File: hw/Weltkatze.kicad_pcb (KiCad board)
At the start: 2 copper layers, 120 x 120 mm, 13 parts, among them U1 ESP32-C6-MINI-1/U

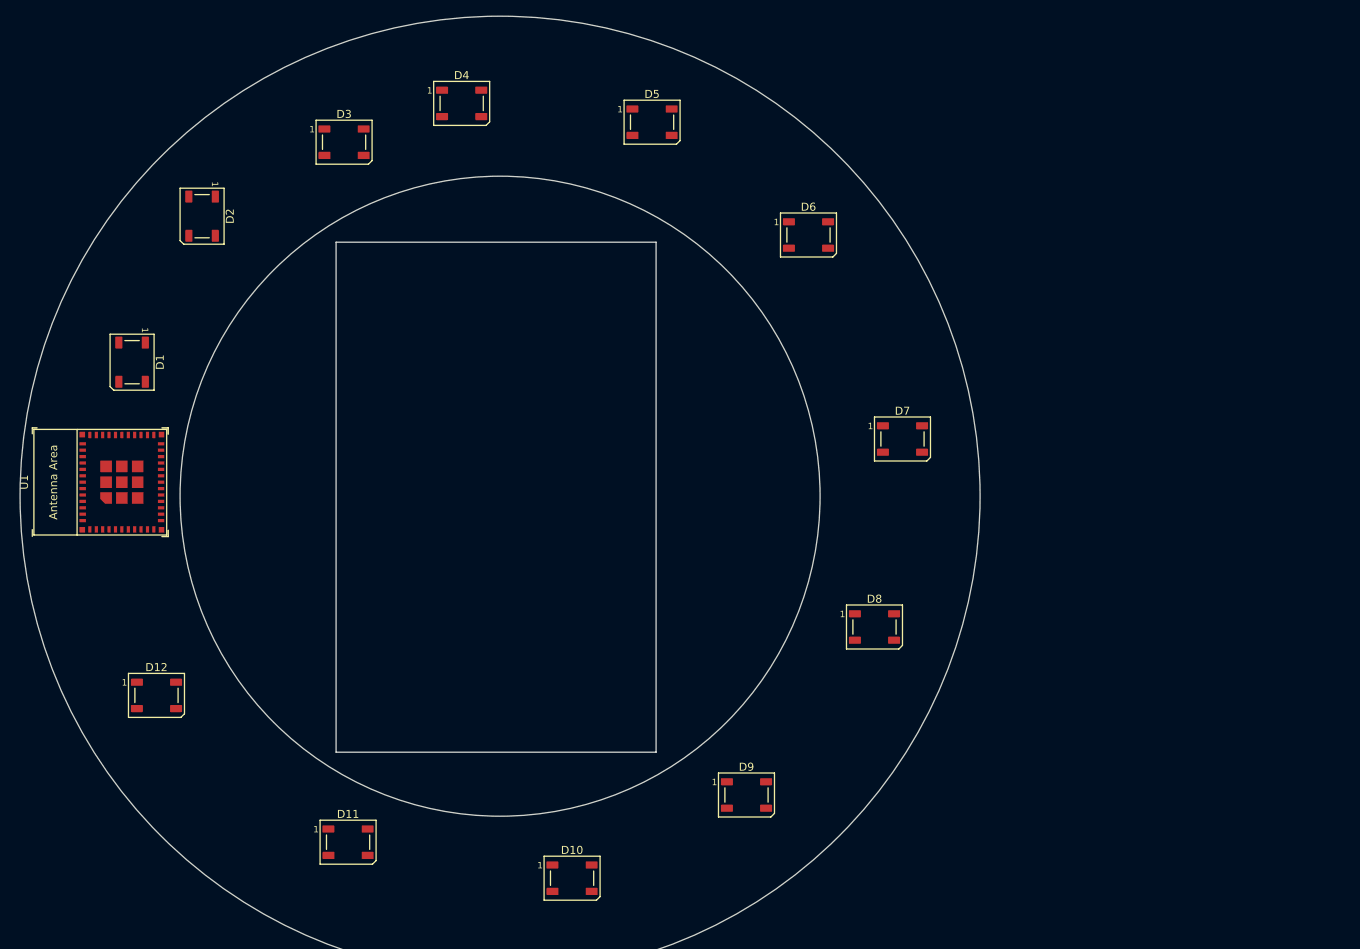
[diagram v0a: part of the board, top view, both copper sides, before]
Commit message: Work on footprinting and PCB
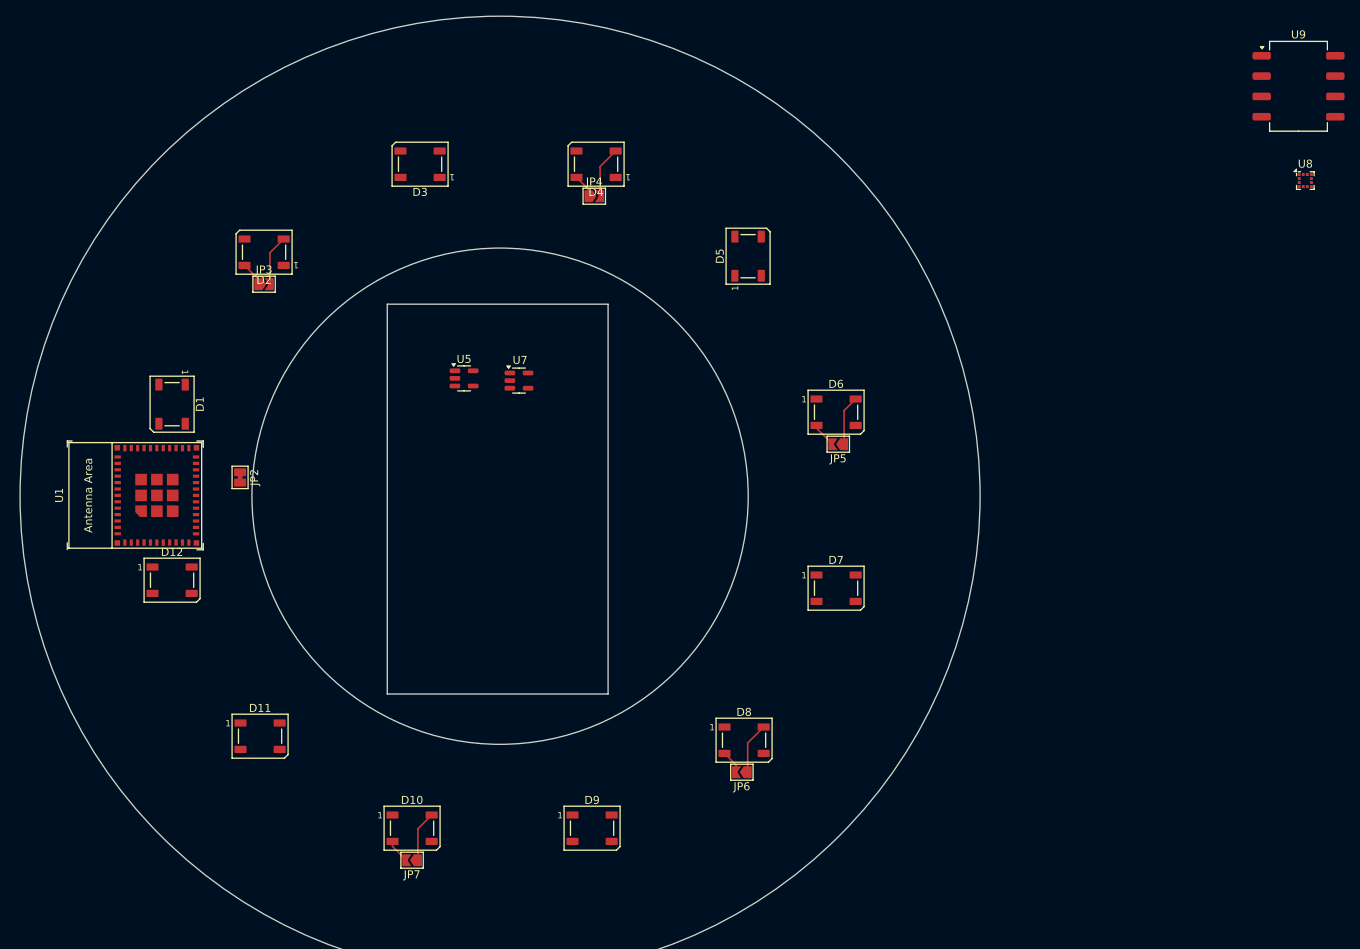
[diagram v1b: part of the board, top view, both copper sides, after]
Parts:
- added JP2: DBG_UART, Jumper:SolderJumper-2_P1.3mm_Bridged_Pad1.0x1.5mm, F.Cu at (98.5, 99.2)
- added JP3: SolderJumper_2_Open, Jumper:SolderJumper-2_P1.3mm_Open_TrianglePad1.0x1.5mm, F.Cu at (101.5, 75.0)
- added JP4: SolderJumper_2_Open, Jumper:SolderJumper-2_P1.3mm_Open_TrianglePad1.0x1.5mm, F.Cu at (142.8, 64.0)
- added JP5: SolderJumper_2_Open, Jumper:SolderJumper-2_P1.3mm_Open_TrianglePad1.0x1.5mm, F.Cu at (173.3, 95.0)
- added JP6: SolderJumper_2_Open, Jumper:SolderJumper-2_P1.3mm_Open_TrianglePad1.0x1.5mm, F.Cu at (161.2, 136.0)
- added JP7: SolderJumper_2_Open, Jumper:SolderJumper-2_P1.3mm_Open_TrianglePad1.0x1.5mm, F.Cu at (120.0, 147.0)
- added U5: SPX3819M5-L-3-3, Package_TO_SOT_SMD:SOT-23-5, F.Cu at (126.5, 86.8)
- added U7: SPX3819M5-L-3-3, Package_TO_SOT_SMD:SOT-23-5, F.Cu at (133.4, 87.0)
- added U8: SC7A20, Package_LGA:LGA-12_2x2mm_P0.5mm, F.Cu at (231.7, 62.0)
- added U9: XGZP6897D, Sensor_Pressure:CFSensor_XGZP6897x, F.Cu at (230.8, 50.3)
- moved D6 22.4 mm to (173.0, 91.0)
- moved D8 21.6 mm to (161.5, 132.0)
- moved D10 21.0 mm to (120.0, 143.0)
- moved D5 20.6 mm to (162.0, 71.5), turned to 90 degrees
- moved D7 20.4 mm to (173.0, 113.0)
- moved D9 19.7 mm to (142.5, 143.0)
- moved D4 18.4 mm to (143.0, 60.0), turned to 180 degrees
- moved D11 17.2 mm to (101.0, 131.5)
- moved D12 14.5 mm to (90.0, 112.0)
- moved D3 9.89 mm to (121.0, 60.0), turned to 180 degrees
- moved D2 8.96 mm to (101.5, 71.0), turned to 180 degrees
- moved D1 7.25 mm to (90.0, 90.0)
- moved U1 4.68 mm to (85.4, 101.4)
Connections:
- net /LEDs/5V renamed +5V
- net Net-(U1-EN/CHIP_PU) renamed /Logic/ESP_RST
- D12 pad 2: unconnected-(D12-DOUT-Pad2) -> Net-(D12-DOUT)
- U1 pad 10: unconnected-(U1-MTDI/GPIO5/ADC1_CH5-Pad10) -> Net-(J3-Pin_3)
- U1 pad 12: unconnected-(U1-GPIO0/ADC1_CH0/XTAL_32K_P-Pad12) -> /Logic/XTAL_P
- U1 pad 13: unconnected-(U1-GPIO1/ADC1_CH1/XTAL_32K_N-Pad13) -> /Logic/XTAL_N
- U1 pad 15: unconnected-(U1-MTCK/GPIO6/ADC1_CH6-Pad15) -> Net-(J3-Pin_2)
- U1 pad 16: unconnected-(U1-MTDO/GPIO7-Pad16) -> Net-(J3-Pin_1)
- U1 pad 17: unconnected-(U1-GPIO12/USB_D--Pad17) -> /Logic/USB_DM
- U1 pad 18: unconnected-(U1-GPIO13/USB_D+-Pad18) -> /Logic/USB_DP
- U1 pad 19: unconnected-(U1-GPIO14-Pad19) -> /Logic/ESP_SCL
- U1 pad 20: unconnected-(U1-GPIO15-Pad20) -> /Logic/ESP_SDA
- U1 pad 22: unconnected-(U1-GPIO8-Pad22) -> Net-(U1-GPIO8)
- U1 pad 23: unconnected-(U1-GPIO9-Pad23) -> /Logic/ESP_BOOT
- U1 pad 28: unconnected-(U1-GPIO22-Pad28) -> /LEDs/LED_DIN
- U1 pad 30: unconnected-(U1-U0RXD/GPIO17-Pad30) -> /Logic/UART_RX
- U1 pad 31: unconnected-(U1-U0TXD/GPIO16-Pad31) -> /Logic/UART_TX
- U1 pad 6: unconnected-(U1-GPIO3/ADC1_CH3-Pad6) -> /Logic/VBAT_MON
- U1 pad 9: unconnected-(U1-MTMS/GPIO4/ADC1_CH4-Pad9) -> Net-(J3-Pin_4)
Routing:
- net Net-(D7-DOUT): track 0.00 -> 6.48 mm
- net Net-(D4-DOUT): track 0.00 -> 6.46 mm
- net Net-(D10-DIN): track 0.00 -> 6.36 mm
- net Net-(D2-DOUT): track 0.00 -> 6.36 mm
- net Net-(D5-DOUT): track 0.00 -> 6.25 mm
- net Net-(D6-DOUT): track 0.00 -> 3.18 mm
- net Net-(D10-DOUT): track 0.00 -> 3.06 mm
- net Net-(D1-DOUT): track 0.00 -> 3.06 mm
- net Net-(D3-DOUT): track 0.00 -> 2.97 mm
- net Net-(D8-DOUT): track 0.00 -> 2.95 mm
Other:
- outline, holes or cut-outs redrawn

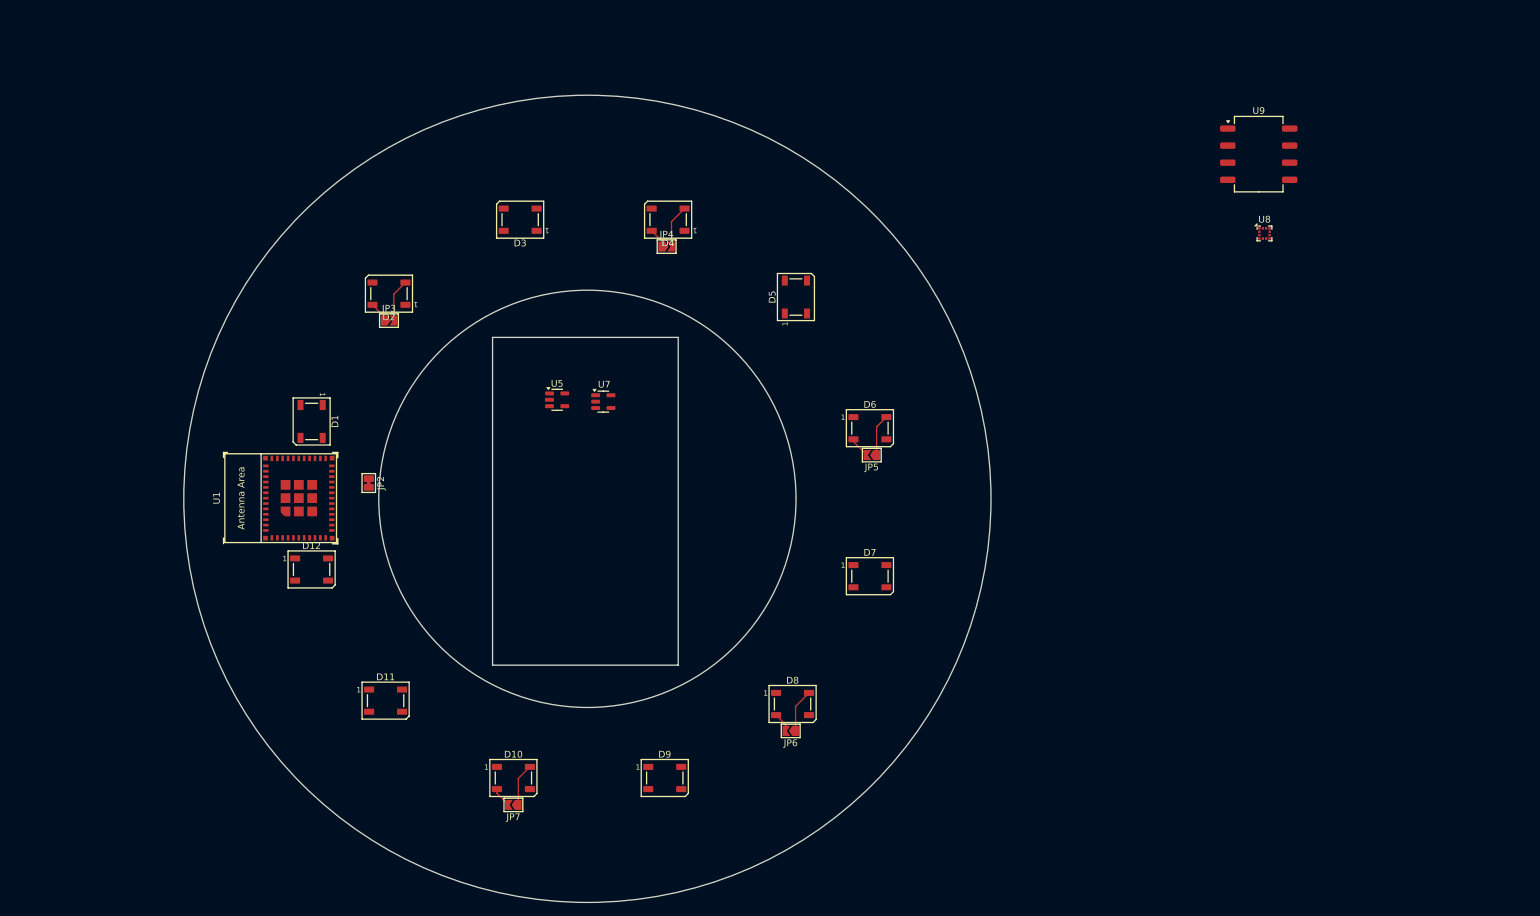
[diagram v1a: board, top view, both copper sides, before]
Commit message: Footprinting, begin layout
I've assigned all the footprints except a few, so I've started on layout.
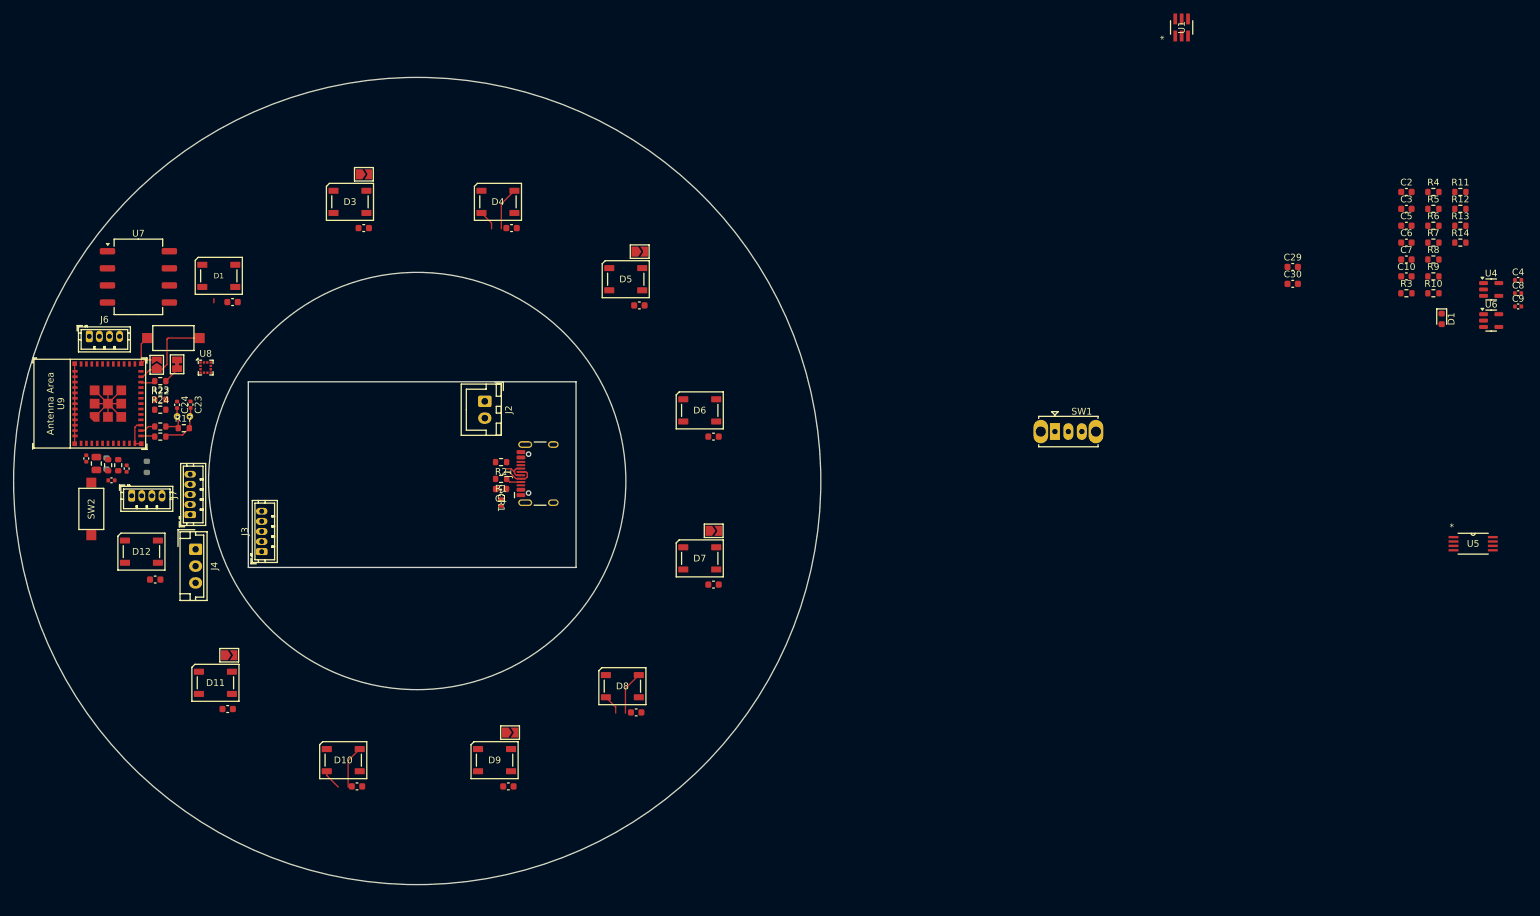
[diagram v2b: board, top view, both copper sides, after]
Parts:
- added C1: 10u, Capacitor_SMD:C_0603_1608Metric, F.Cu at (118.2, 100.0)
- added C10: 10u, Capacitor_SMD:C_0603_1608Metric, F.Cu at (252.8, 68.4)
- added C11: 10u, Capacitor_SMD:C_0603_1608Metric, F.Cu at (78.2, 72.2)
- added C12: 10u, Capacitor_SMD:C_0603_1608Metric, F.Cu at (97.8, 61.2)
- added C13: 10u, Capacitor_SMD:C_0603_1608Metric, F.Cu at (119.7, 61.2)
- added C14: 10u, Capacitor_SMD:C_0603_1608Metric, F.Cu at (138.7, 72.8)
- added C15: 10u, Capacitor_SMD:C_0603_1608Metric, F.Cu at (149.8, 92.2)
- added C16: 10u, Capacitor_SMD:C_0603_1608Metric, F.Cu at (149.8, 114.2)
- added C17: 10u, Capacitor_SMD:C_0603_1608Metric, F.Cu at (138.2, 133.2)
- added C18: 10u, Capacitor_SMD:C_0603_1608Metric, F.Cu at (119.2, 144.2)
- added C19: 10u, Capacitor_SMD:C_0603_1608Metric, F.Cu at (96.8, 144.2)
- added C2: 10u, Capacitor_SMD:C_0603_1608Metric, F.Cu at (252.8, 55.9)
- added C20: 10u, Capacitor_SMD:C_0603_1608Metric, F.Cu at (77.5, 132.8)
- added C21: 10u, Capacitor_SMD:C_0603_1608Metric, F.Cu at (66.8, 113.5)
- added C23: 12p, Capacitor_SMD:C_0402_1005Metric, F.Cu at (72.0, 87.5)
- added C24: 12p, Capacitor_SMD:C_0402_1005Metric, F.Cu at (70.0, 87.5)
- added C25: 0.1u, Capacitor_SMD:C_0402_1005Metric, F.Cu at (60.2, 98.8)
- added C26: 0.1u, Capacitor_SMD:C_0402_1005Metric, F.Cu at (62.5, 97.0)
- added C27: 22u, Capacitor_SMD:C_0805_2012Metric, F.Cu at (58.0, 96.2)
- added C28: 0.1u, Capacitor_SMD:C_0402_1005Metric, F.Cu at (56.5, 95.5)
- added C29: 0.1u, Capacitor_SMD:C_0603_1608Metric, F.Cu at (235.9, 67.0)
- added C3: 10u, Capacitor_SMD:C_0603_1608Metric, F.Cu at (252.8, 58.4)
- added C30: 0.1u, Capacitor_SMD:C_0603_1608Metric, F.Cu at (235.9, 69.5)
- added C4: 0.1u, Capacitor_SMD:C_0402_1005Metric, F.Cu at (269.4, 69.0)
- added C5: 10u, Capacitor_SMD:C_0603_1608Metric, F.Cu at (252.8, 60.9)
- added C6: 10u, Capacitor_SMD:C_0603_1608Metric, F.Cu at (252.8, 63.4)
- added C7: 10u, Capacitor_SMD:C_0603_1608Metric, F.Cu at (252.8, 65.9)
- added C8: 0.1u, Capacitor_SMD:C_0402_1005Metric, F.Cu at (269.4, 70.9)
- added C9: 0.1u, Capacitor_SMD:C_0402_1005Metric, F.Cu at (269.4, 72.9)
- added CR1: ESDA25P35-1U1M, lib:QFN1610_STM-M, F.Cu at (118.2, 102.1)
- added J1: USB_C_Receptacle_USB2.0_14P, Connector_USB:USB_C_Receptacle_HCTL_HC-TYPE-C-16P-01A, F.Cu at (124.9, 97.8)
- added J2: CONN_BAT, Connector_JST:JST_XH_B2B-XH-A_1x02_P2.50mm_Vertical, F.Cu at (115.8, 87.0)
- added J3: PWR, Connector_JST:JST_ZH_B5B-ZR_1x05_P1.50mm_Vertical, F.Cu at (82.6, 109.3)
- added J4: LED_OUT, Connector_JST:JST_EH_B3B-EH-A_1x03_P2.50mm_Vertical, F.Cu at (72.8, 109.0)
- added J5: JTAG, Connector_JST:JST_ZH_B4B-ZR_1x04_P1.50mm_Vertical, F.Cu at (63.2, 101.0)
- added J6: UART, Connector_JST:JST_ZH_B4B-ZR_1x04_P1.50mm_Vertical, F.Cu at (57.0, 77.3)
- added J7: ESP_PWR, Connector_JST:JST_ZH_B5B-ZR_1x05_P1.50mm_Vertical, F.Cu at (71.9, 103.8)
- added JP1: SolderJumper_2_Open, Jumper:SolderJumper-2_P1.3mm_Open_TrianglePad1.0x1.5mm, F.Cu at (97.8, 53.2)
- added R1: 5.1k, Resistor_SMD:R_0603_1608Metric, F.Cu at (118.2, 98.5)
- added R10: 100k, Resistor_SMD:R_0603_1608Metric, F.Cu at (256.8, 70.9)
- added R11: 732k, Resistor_SMD:R_0603_1608Metric, F.Cu at (260.8, 55.9)
- added R12: 1k, Resistor_SMD:R_0603_1608Metric, F.Cu at (260.8, 58.4)
- added R13: 470, Resistor_SMD:R_0603_1608Metric, F.Cu at (260.8, 60.9)
- added R14: 191, Resistor_SMD:R_0603_1608Metric, F.Cu at (260.8, 63.4)
- added R15: 200k, Resistor_SMD:R_0603_1608Metric, B.Cu at (65.5, 96.8)
- added R16: 200k, Resistor_SMD:R_0603_1608Metric, B.Cu at (59.5, 96.2)
- added R17: 0, Resistor_SMD:R_0603_1608Metric, F.Cu at (71.0, 91.0)
- added R18: 0, Resistor_SMD:R_0603_1608Metric, F.Cu at (67.5, 92.2)
- added R19: 0, Resistor_SMD:R_0603_1608Metric, F.Cu at (67.5, 90.8)
- added R2: 5.1k, Resistor_SMD:R_0603_1608Metric, F.Cu at (118.2, 96.0)
- added R20: 0, Resistor_SMD:R_0603_1608Metric, F.Cu at (61.2, 96.5)
- added R21: 10k, Resistor_SMD:R_0603_1608Metric, F.Cu at (59.8, 96.5)
- added R22: 10k, Resistor_SMD:R_0603_1608Metric, F.Cu at (67.5, 84.0)
- added R23: 0, Resistor_SMD:R_0603_1608Metric, F.Cu at (67.5, 86.8)
- added R24: 0, Resistor_SMD:R_0603_1608Metric, F.Cu at (67.5, 88.2)
- added R3: 597k, Resistor_SMD:R_0603_1608Metric, F.Cu at (252.8, 70.9)
- added R4: 49.9k, Resistor_SMD:R_0603_1608Metric, F.Cu at (256.8, 55.9)
- added R5: 49.9k, Resistor_SMD:R_0603_1608Metric, F.Cu at (256.8, 58.4)
- added R6: 49.9k, Resistor_SMD:R_0603_1608Metric, F.Cu at (256.8, 60.9)
- added R7: 66.5k, Resistor_SMD:R_0603_1608Metric, F.Cu at (256.8, 63.4)
- added R8: 1k, Resistor_SMD:R_0603_1608Metric, F.Cu at (256.8, 65.9)
- added R9: 1.5k, Resistor_SMD:R_0603_1608Metric, F.Cu at (256.8, 68.4)
- added SW1: SW_SPDT, Button_Switch_THT:SW_Slide_SPDT_Straight_CK_OS102011MS2Q, F.Cu at (200.5, 91.5)
- added SW2: SW_Push, Button_Switch_SMD:SW_SPST_CK_RS282G05A3, F.Cu at (57.2, 103.0)
- added SW3: SW_Push, Button_Switch_SMD:SW_SPST_CK_RS282G05A3, F.Cu at (69.5, 77.6)
- added U4: SPX3819M5-L-3-3, Package_TO_SOT_SMD:SOT-23-5, F.Cu at (265.4, 70.4)
- added U6: SPX3819M5-L-3-3, Package_TO_SOT_SMD:SOT-23-5, F.Cu at (265.4, 75.0)
- added Y1: 32.768k, Crystal:Crystal_C26-LF_D2.1mm_L6.5mm_Horizontal, B.Cu at (70.0, 89.2)
- D1: value WS2812B -> R; footprint LED_SMD:LED_WS2812B_PLCC4_5.0x5.0mm_P3.2mm -> LED_SMD:LED_0603_1608Metric
- JP2: value DBG_UART -> SolderJumper_2_Open; footprint Jumper:SolderJumper-2_P1.3mm_Bridged_Pad1.0x1.5mm -> Jumper:SolderJumper-2_P1.3mm_Open_TrianglePad1.0x1.5mm
- JP6: value SolderJumper_2_Open -> DBG_UART; footprint Jumper:SolderJumper-2_P1.3mm_Open_TrianglePad1.0x1.5mm -> Jumper:SolderJumper-2_P1.3mm_Bridged_Pad1.0x1.5mm
- U1: value ESP32-C6-MINI-1/U -> TPS3700DDCR; footprint PCM_Espressif:ESP32-C6-MINI-1 -> lib:DDC6_TEX-M
- U5: value SPX3819M5-L-3-3 -> TPS2111APW; footprint Package_TO_SOT_SMD:SOT-23-5 -> lib:PW8
- U7: value SPX3819M5-L-3-3 -> XGZP6897D; footprint Package_TO_SOT_SMD:SOT-23-5 -> Sensor_Pressure:CFSensor_XGZP6897x
- U9: value XGZP6897D -> ESP32-C6-MINI-1/U; footprint Sensor_Pressure:CFSensor_XGZP6897x -> PCM_Espressif:ESP32-C6-MINI-1
- moved U9 177.7 mm to (57.0, 87.3), turned to 90 degrees
- moved D1 168.7 mm to (258.0, 74.8)
- moved U8 158.7 mm to (74.2, 82.0)
- moved U1 151.1 mm to (219.3, 31.4)
- moved U5 137.8 mm to (262.7, 108.2)
- moved JP6 106.3 mm to (70.0, 81.5), turned to 90 degrees
- moved JP5 100.1 mm to (77.8, 124.8), turned to 0 degrees
- moved JP7 84.2 mm to (67.0, 81.6), turned to 90 degrees
- moved JP4 75.9 mm to (119.5, 136.2)
- moved U7 71.6 mm to (64.2, 68.5)
- moved JP3 57.5 mm to (149.8, 106.2)
- moved JP2 53.0 mm to (138.8, 64.8), turned to 0 degrees
- moved D5 25.4 mm to (136.7, 68.8), turned to 180 degrees
- moved D6 25.4 mm to (147.7, 88.3), turned to 180 degrees
- moved D7 25.4 mm to (147.7, 110.3), turned to 180 degrees
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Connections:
- D1 pad 1: +5V -> Net-(D1-K)
- D1 pad 2: Net-(D1-DOUT) -> /Power/USB_VBUS
- D2 pad 4: Net-(D1-DOUT) -> /LEDs/LED_DIN
- JP2 pad 1: Net-(JP2-A) -> Net-(D4-DOUT)
- JP2 pad 2: +3V3 -> Net-(D5-DOUT)
- JP3 pad 1: Net-(D1-DOUT) -> Net-(D6-DOUT)
- JP3 pad 2: Net-(D2-DOUT) -> Net-(D7-DOUT)
- JP4 pad 1: Net-(D3-DOUT) -> Net-(D8-DOUT)
- JP4 pad 2: Net-(D4-DOUT) -> Net-(D10-DIN)
- JP5 pad 1: Net-(D5-DOUT) -> Net-(D10-DOUT)
- JP5 pad 2: Net-(D6-DOUT) -> Net-(D11-DOUT)
- JP6 pad 1: Net-(D7-DOUT) -> Net-(JP6-A)
- JP6 pad 2: Net-(D8-DOUT) -> +3V3
- JP7 pad 1: Net-(D10-DIN) -> /Logic/ESP_BOOT
- JP7 pad 2: Net-(D10-DOUT) -> GND
- U1 pad 1: GND -> /Power/VBAT_EN
- U1 pad 3: +3V3 -> Net-(U1-INA+)
- U1 pad 4: unconnected-(U1-NC-Pad4) -> Net-(U1-INB-)
- U1 pad 5: unconnected-(U1-GPIO2/ADC1_CH2-Pad5) -> /Power/VBAT_SW
- U1 pad 6: /Logic/VBAT_MON -> /Power/VBAT_EN
- U5 pad 1: /Power/VBAT_SW -> unconnected-(U5-D0-Pad1)
- U5 pad 3: /Power/VBAT_EN -> Net-(U5-VSNS)
- U5 pad 4: unconnected-(U5-BP-Pad4) -> Net-(U5-ILIM)
- U5 pad 5: +3V3 -> GND
- U7 pad 1: +5V -> unconnected-(U7-NC-Pad1)
- U7 pad 2: GND -> unconnected-(U7-VDD-Pad2)
- U7 pad 3: +5V -> unconnected-(U7-NC-Pad3)
- U7 pad 5: +3V3 -> unconnected-(U7-NC-Pad5)
- U9 pad 1: unconnected-(U9-NC-Pad1) -> GND
- U9 pad 2: unconnected-(U9-VDD-Pad2) -> GND
- U9 pad 3: unconnected-(U9-NC-Pad3) -> +3V3
- U9 pad 6: unconnected-(U9-SDA-Pad6) -> /Logic/VBAT_MON
- U9 pad 8: unconnected-(U9-GND-Pad8) -> /Logic/ESP_RST
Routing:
- net GND: track 0.00 -> 42.1 mm
- net /Logic/ESP_BOOT: track 0.00 -> 13.3 mm
- net Net-(C23-Pad2): track 0.00 -> 7.11 mm
- net Net-(D2-DOUT): track 6.36 -> 0.00 mm
- net Net-(D5-DOUT): track 6.25 -> 0.35 mm
- net /Logic/ESP_DN: track 0.00 -> 5.23 mm
- net Net-(C24-Pad2): track 0.00 -> 5.03 mm
- net /Logic/ESP_DP: track 0.00 -> 4.04 mm
- net Net-(D7-DOUT): track 6.48 -> 2.95 mm
- net Net-(D8-DOUT): track 2.95 -> 6.48 mm
- net Net-(D10-DIN): track 6.36 -> 3.06 mm
- net Net-(D10-DOUT): track 3.06 -> 6.36 mm
- net Net-(D6-DOUT): track 3.18 -> 0.00 mm
- net Net-(D1-DOUT): track 3.06 -> 0.00 mm
- net Net-(JP6-A): track 0.00 -> 2.54 mm
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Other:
- outline, holes or cut-outs redrawn
- board text added: "JLCJLCJLCJLC"

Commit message: yes
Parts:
- added C22: 10u, Capacitor_SMD:C_0603_1608Metric, F.Cu at (67.0, 91.8)
- added D13: WS2812B, LED_SMD:LED_WS2812B_PLCC4_5.0x5.0mm_P3.2mm, F.Cu at (64.8, 87.2)
- added JP8: SolderJumper_2_Open, Jumper:SolderJumper-2_P1.3mm_Open_TrianglePad1.0x1.5mm, F.Cu at (62.8, 91.2)
- added U2: TP4056, lib:SOP127P600X175-9N, F.Cu at (199.0, 77.8)
- added U3: TPS61023DRLR, lib:DRL0006A, F.Cu at (195.4, 82.6)
- moved C1 143.0 mm to (253.8, 145.3)
- moved C23 143.0 mm to (207.7, 132.8)
- moved C24 143.0 mm to (205.7, 132.8)
- moved C25 143.0 mm to (195.9, 144.0)
- moved C26 143.0 mm to (198.2, 142.2)
- moved C27 143.0 mm to (193.7, 141.5)
- moved C28 143.0 mm to (192.2, 140.8)
- moved CR1 143.0 mm to (253.8, 147.3)
- moved J1 143.0 mm to (260.5, 143.0)
- moved J2 143.0 mm to (251.4, 132.2)
- moved J5 143.0 mm to (198.9, 146.3)
- moved J6 143.0 mm to (192.6, 122.6)
- moved J7 143.0 mm to (207.6, 149.1)
- moved JP6 143.0 mm to (205.7, 126.8)
- moved JP7 143.0 mm to (202.7, 126.8)
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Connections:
- J4 pad 2: Net-(D12-DOUT) -> Net-(D13-DOUT)
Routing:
- net +5V: track 0.00 -> 60.2 mm
- added copper zone on F.Cu, net GND
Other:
- outline, holes or cut-outs redrawn
